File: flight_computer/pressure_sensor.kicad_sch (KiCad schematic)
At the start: 4 parts, among them U1 SPL07-003

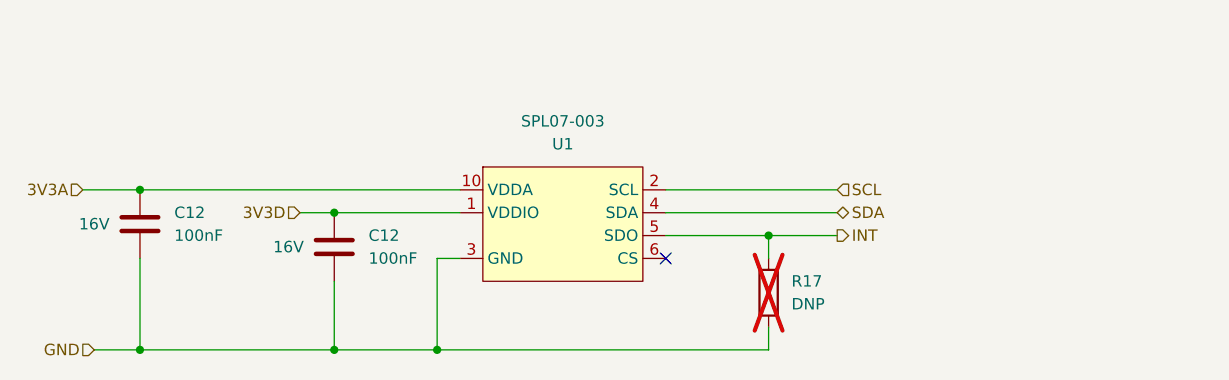
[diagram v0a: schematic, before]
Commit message: Tidying up schematics and adding most missing sections (Not finished GPS)
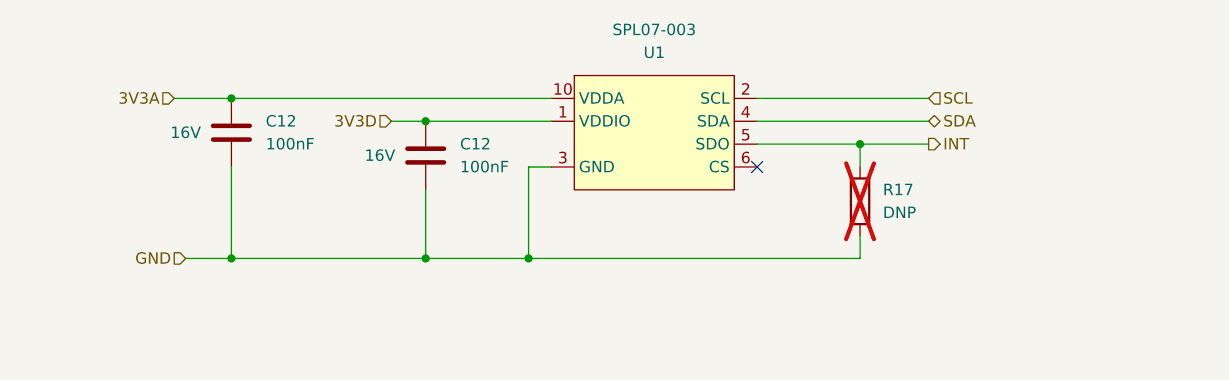
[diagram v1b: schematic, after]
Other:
- moved on the sheet: C12, R17, U1

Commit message: Schematic connecting
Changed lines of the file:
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@@
   )
   (no_connect (at 177.8 87.63))
+  (bus_entry (at 210.82 77.47) (size -2.54 2.54)
+    (stroke (width 0) (type default))
+  )
+  (bus_entry (at 210.82 80.01) (size -2.54 2.54)
+    (stroke (width 0) (type default))
+  )
   (wire (pts (xy 189.23 87.63) (xy 189.23 85.09))
     (stroke (width 0) (type default))
@@
     (stroke (width 0) (type default))
   )
+  (bus (pts (xy 219.71 74.93) (xy 210.82 74.93))
+    (stroke (width 0) (type default))
+  )
   (wire (pts (xy 152.4 97.79) (xy 152.4 87.63))
+    (stroke (width 0) (type default))
+  )
+  (bus (pts (xy 210.82 77.47) (xy 210.82 80.01))
     (stroke (width 0) (type default))
   )
@@
     (stroke (width 0) (type default))
   )
-  (wire (pts (xy 177.8 82.55) (xy 196.85 82.55))
+  (wire (pts (xy 177.8 82.55) (xy 208.28 82.55))
     (stroke (width 0) (type default))
   )
@@
   )
   (wire (pts (xy 113.03 80.01) (xy 119.38 80.01))
+    (stroke (width 0) (type default))
+  )
+  (bus (pts (xy 210.82 74.93) (xy 210.82 77.47))
     (stroke (width 0) (type default))
   )
@@
     (stroke (width 0) (type default))
   )
-  (wire (pts (xy 177.8 80.01) (xy 196.85 80.01))
+  (wire (pts (xy 177.8 80.01) (xy 208.28 80.01))
     (stroke (width 0) (type default))
+  )
+  (label "SCL" (at 204.47 80.01 180) (fields_autoplaced)
+    (effects (font (size 1.27 1.27)) (justify right bottom))
+  )
+  (label "SDA" (at 204.47 82.55 180) (fields_autoplaced)
+    (effects (font (size 1.27 1.27)) (justify right bottom))
   )
   (hierarchical_label "3V3A" (shape input) (at 113.03 80.01 180) (fields_autoplaced)
@@
     (effects (font (size 1.27 1.27)) (justify right))
   )
-  (hierarchical_label "SCL" (shape input) (at 196.85 80.01 0) (fields_autoplaced)
-    (effects (font (size 1.27 1.27)) (justify left))
-  )
   (hierarchical_label "3V3D" (shape input) (at 137.16 82.55 180) (fields_autoplaced)
     (effects (font (size 1.27 1.27)) (justify right))
   )
-  (hierarchical_label "SDA" (shape bidirectional) (at 196.85 82.55 0) (fields_autoplaced)
-    (effects (font (size 1.27 1.27)) (justify left))
+  (hierarchical_label "{I2C}" (shape input) (at 219.71 74.93 0) (fields_autoplaced)
+    (effects (font (size 1.27 1.27) (thickness 0.254) bold) (justify left))
   )
   (symbol (lib_id "Device:R") (at 189.23 91.44 0) (unit 1)

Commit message: Part way through review
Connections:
- net 3V3A renamed 1V8A
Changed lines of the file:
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@@
     (effects (font (size 1.27 1.27)) (justify right bottom))
-  )
-  (hierarchical_label "3V3A" (shape input) (at 113.03 80.01 180) (fields_autoplaced)
-    (effects (font (size 1.27 1.27)) (justify right))
   )
   (hierarchical_label "INT" (shape output) (at 196.85 85.09 0) (fields_autoplaced)
@@
   )
   (hierarchical_label "3V3D" (shape input) (at 137.16 82.55 180) (fields_autoplaced)
+    (effects (font (size 1.27 1.27)) (justify right))
+  )
+  (hierarchical_label "1V8A" (shape input) (at 113.03 80.01 180) (fields_autoplaced)
     (effects (font (size 1.27 1.27)) (justify right))
   )
@@
       (effects (font (size 1.27 1.27)) hide)
     )
-    (property "Manufacturer PN" "" (at 189.23 91.44 0)
+    (property "Manufacturer PN" "~" (at 189.23 91.44 0)
       (effects (font (size 1.27 1.27)) hide)
     )
-    (property "Supplier PN" "" (at 189.23 91.44 0)
+    (property "Supplier PN" "~" (at 189.23 91.44 0)
       (effects (font (size 1.27 1.27)) hide)
     )
-    (property "Supplier" "" (at 189.23 91.44 0)
+    (property "Supplier" "~" (at 189.23 91.44 0)
       (effects (font (size 1.27 1.27)) hide)
     )
@@
         )
         (path "/89a81c02-14e9-456f-a334-ff69a24bd093/c81a97f0-01ba-4e2a-b4b2-3d08d9bf2671"
-          (reference "C16") (unit 1)
+          (reference "C17") (unit 1)
         )
       )
@@
         )
         (path "/89a81c02-14e9-456f-a334-ff69a24bd093/c81a97f0-01ba-4e2a-b4b2-3d08d9bf2671"
-          (reference "C15") (unit 1)
+          (reference "C16") (unit 1)
         )
       )

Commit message: Start of layout
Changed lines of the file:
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@@
 (kicad_sch (version 20230121) (generator eeschema)
   (paper "A4")
-  (junction (at 152.4 97.79) (diameter 0) (color 0 0 0 0)
+  (junction (at 119.38 80.01) (diameter 0) (color 0 0 0 0)
   )
-  (junction (at 119.38 80.01) (diameter 0) (color 0 0 0 0)
+  (junction (at 163.83 97.79) (diameter 0) (color 0 0 0 0)
   )
   (junction (at 189.23 85.09) (diameter 0) (color 0 0 0 0)
@@
   (junction (at 140.97 97.79) (diameter 0) (color 0 0 0 0)
   )
+  (junction (at 166.37 97.79) (diameter 0) (color 0 0 0 0)
+  )
   (junction (at 140.97 82.55) (diameter 0) (color 0 0 0 0)
+  )
+  (junction (at 168.91 97.79) (diameter 0) (color 0 0 0 0)
   )
   (junction (at 119.38 97.79) (diameter 0) (color 0 0 0 0)
@@
     (stroke (width 0) (type default))
   )
-  (wire (pts (xy 152.4 87.63) (xy 154.94 87.63))
+  (wire (pts (xy 177.8 85.09) (xy 189.23 85.09))
     (stroke (width 0) (type default))
   )
-  (wire (pts (xy 177.8 85.09) (xy 189.23 85.09))
+  (wire (pts (xy 166.37 97.79) (xy 168.91 97.79))
     (stroke (width 0) (type default))
   )
@@
     (stroke (width 0) (type default))
   )
-  (wire (pts (xy 152.4 97.79) (xy 152.4 87.63))
+  (wire (pts (xy 166.37 92.71) (xy 166.37 97.79))
     (stroke (width 0) (type default))
   )
@@
     (stroke (width 0) (type default))
   )
-  (wire (pts (xy 140.97 97.79) (xy 152.4 97.79))
+  (wire (pts (xy 140.97 97.79) (xy 163.83 97.79))
     (stroke (width 0) (type default))
   )
@@
     (stroke (width 0) (type default))
   )
-  (wire (pts (xy 189.23 97.79) (xy 152.4 97.79))
+  (wire (pts (xy 113.03 80.01) (xy 119.38 80.01))
     (stroke (width 0) (type default))
   )
-  (wire (pts (xy 113.03 80.01) (xy 119.38 80.01))
+  (wire (pts (xy 163.83 92.71) (xy 163.83 97.79))
     (stroke (width 0) (type default))
   )
@@
     (stroke (width 0) (type default))
   )
+  (wire (pts (xy 168.91 97.79) (xy 189.23 97.79))
+    (stroke (width 0) (type default))
+  )
   (wire (pts (xy 137.16 82.55) (xy 140.97 82.55))
     (stroke (width 0) (type default))
   )
+  (wire (pts (xy 168.91 92.71) (xy 168.91 97.79))
+    (stroke (width 0) (type default))
+  )
+  (wire (pts (xy 163.83 97.79) (xy 166.37 97.79))
+    (stroke (width 0) (type default))
+  )
